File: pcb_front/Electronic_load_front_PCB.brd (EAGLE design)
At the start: 33 x 46.7 mm, 9 parts, among them SW1 EC12E_SW

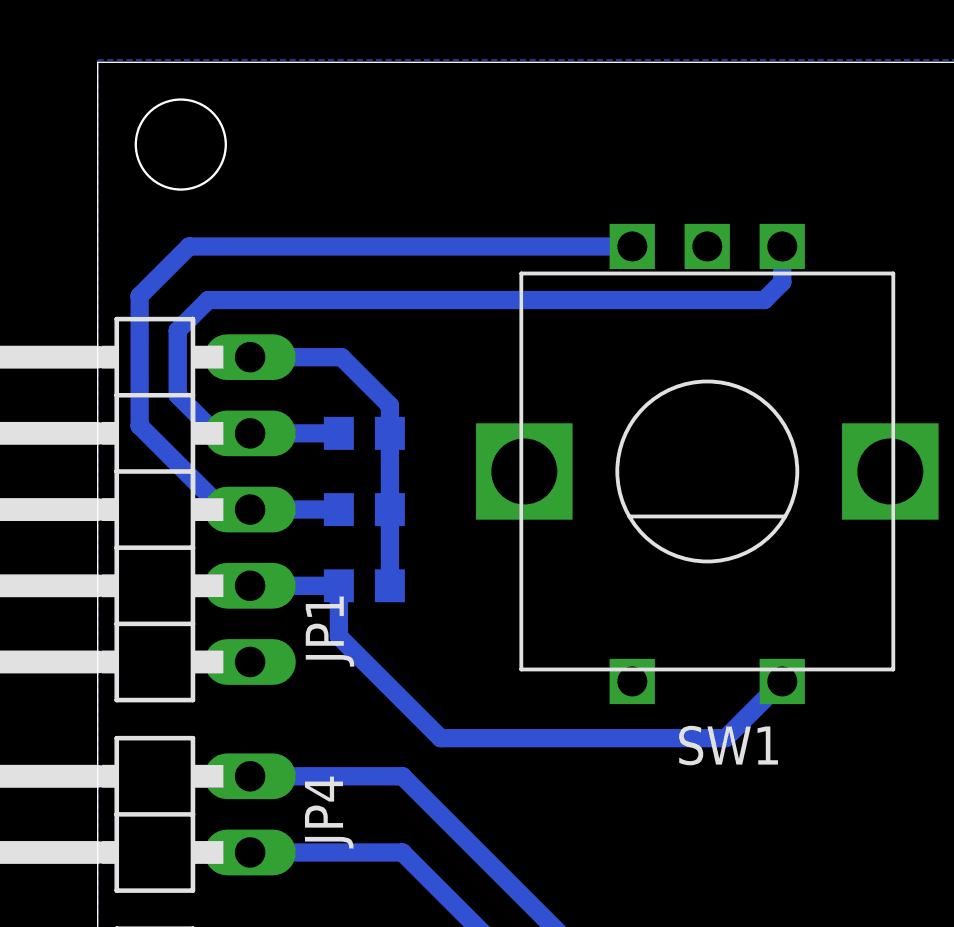
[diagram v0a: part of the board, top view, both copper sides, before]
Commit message: encoder works great, bounces reduced
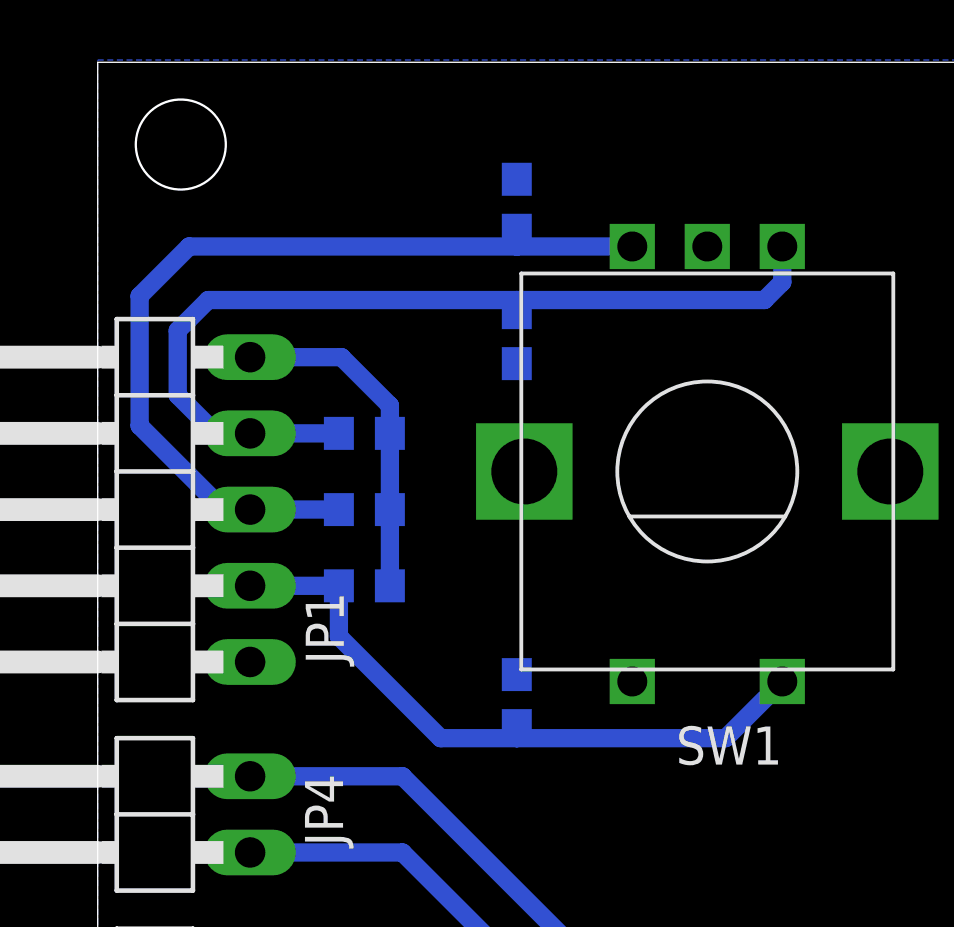
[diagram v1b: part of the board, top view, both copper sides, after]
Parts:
- added C1, C2, C3: 100n, rcl:C0603
- R1, R2: value (none) -> 4k7
- R3: value (none) -> 12k
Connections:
- net ENC_A: now also C2.1
- net ENC_B: now also C3.1
- net ENC_SW: now also C1.1
- net GND: now also C1.2, C2.2, C3.2
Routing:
- net ENC_A: track 29.2 -> 29.8 mm
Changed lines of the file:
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@@
 </layers>
 <board>
-<fusionsync huburn="a.YnVzaW5lc3M6Z21haWw1MzQ2MjM" projecturn="a.YnVzaW5lc3M6Z21haWw1MzQ2MjMjRDIwMTkxMjI5MjUwNjU0MjU2" f3durn="urn:adsk.wipprod:dm.lineage:3ZborseaTM63qMjKJInqhQ" pcbguid="" lastpulledtime="" lastsyncedchangeguid="" latestrevisionid="de9a6022-fa4f-43a6-98fc-7768da42b81b" lastsyncedrevisionid="de9a6022-fa4f-43a6-98fc-7768da42b81b" lastboardhashguid="187d4fe6-ef17-b919-9e19-ddac4a4cb30f" lastpushedtime="2022-08-03T22:12:43Z" linktopcb3d="true"/>
+<fusionsync huburn="a.YnVzaW5lc3M6Z21haWw1MzQ2MjM" projecturn="a.YnVzaW5lc3M6Z21haWw1MzQ2MjMjRDIwMTkxMjI5MjUwNjU0MjU2" f3durn="urn:adsk.wipprod:dm.lineage:3ZborseaTM63qMjKJInqhQ" pcbguid="" lastpulledtime="" lastsyncedchangeguid="" latestrevisionid="de9a6022-fa4f-43a6-98fc-7768da42b81b" lastsyncedrevisionid="de9a6022-fa4f-43a6-98fc-7768da42b81b" lastboardhashguid="187d4fe6-ef17-b919-9e19-ddac4a4cb30f" lastpushedtime="2022-08-03T22:12:43Z" linktopcb3d="false"/>
 <plain>
 <wire x1="0" y1="0" x2="33" y2="0" width="0" layer="20"/>
@@
 <attribute name="VALUE" x="4.445" y="25.4" size="1.27" layer="27" rot="R90"/>
 </element>
-<element name="R1" library="rcl" library_urn="urn:adsk.eagle:library:334" package="R0603" package3d_urn="urn:adsk.eagle:package:23555/3" value="" x="8.89" y="34.29" smashed="yes" rot="MR180">
+<element name="R1" library="rcl" library_urn="urn:adsk.eagle:library:334" package="R0603" package3d_urn="urn:adsk.eagle:package:23555/3" value="4k7" x="8.89" y="34.29" smashed="yes" rot="MR180">
 <attribute name="NAME" x="10.414" y="34.925" size="1.27" layer="26" rot="MR180"/>
 <attribute name="POPULARITY" value="70" x="8.89" y="34.29" size="1.778" layer="28" rot="MR180" display="off"/>
@@
 <attribute name="VALUE" x="8.255" y="36.195" size="1.27" layer="28" rot="MR180"/>
 </element>
-<element name="R2" library="rcl" library_urn="urn:adsk.eagle:library:334" package="R0603" package3d_urn="urn:adsk.eagle:package:23555/3" value="" x="8.89" y="31.75" smashed="yes" rot="MR180">
+<element name="R2" library="rcl" library_urn="urn:adsk.eagle:library:334" package="R0603" package3d_urn="urn:adsk.eagle:package:23555/3" value="4k7" x="8.89" y="31.75" smashed="yes" rot="MR180">
 <attribute name="NAME" x="10.414" y="32.385" size="1.27" layer="26" rot="MR180"/>
 <attribute name="POPULARITY" value="70" x="8.89" y="31.75" size="1.778" layer="28" rot="MR180" display="off"/>
@@
 <attribute name="VALUE" x="8.255" y="33.655" size="1.27" layer="28" rot="MR180"/>
 </element>
-<element name="R3" library="rcl" library_urn="urn:adsk.eagle:library:334" package="R0603" package3d_urn="urn:adsk.eagle:package:23555/3" value="" x="8.89" y="29.21" smashed="yes" rot="MR180">
+<element name="R3" library="rcl" library_urn="urn:adsk.eagle:library:334" package="R0603" package3d_urn="urn:adsk.eagle:package:23555/3" value="12k" x="8.89" y="29.21" smashed="yes" rot="MR180">
 <attribute name="NAME" x="10.414" y="29.845" size="1.27" layer="26" rot="MR180"/>
 <attribute name="POPULARITY" value="70" x="8.89" y="29.21" size="1.778" layer="28" rot="MR180" display="off"/>
@@
 <attribute name="POPULARITY" value="24" x="1.27" y="21.59" size="1.778" layer="27" rot="R90" display="off"/>
 <attribute name="VALUE" x="4.445" y="19.05" size="1.27" layer="27" rot="R90"/>
+</element>
+<element name="C1" library="rcl" library_urn="urn:adsk.eagle:library:334" package="C0603" package3d_urn="urn:adsk.eagle:package:23616/2" value="100n" x="13.97" y="25.4" smashed="yes" rot="MR90">
+<attribute name="NAME" x="11.811" y="24.257" size="1.27" layer="26" rot="MR90"/>
+<attribute name="POPULARITY" value="73" x="13.97" y="25.4" size="1.778" layer="28" rot="MR90" display="off"/>
+<attribute name="SPICEPREFIX" value="C" x="13.97" y="25.4" size="1.778" layer="28" rot="MR90" display="off"/>
+<attribute name="VALUE" x="12.065" y="24.765" size="1.27" layer="28" rot="MR90"/>
+</element>
+<element name="C2" library="rcl" library_urn="urn:adsk.eagle:library:334" package="C0603" package3d_urn="urn:adsk.eagle:package:23616/2" value="100n" x="13.97" y="41.91" smashed="yes" rot="MR90">
+<attribute name="NAME" x="11.811" y="40.767" size="1.27" layer="26" rot="MR90"/>
+<attribute name="POPULARITY" value="73" x="13.97" y="41.91" size="1.778" layer="28" rot="MR90" display="off"/>
+<attribute name="SPICEPREFIX" value="C" x="13.97" y="41.91" size="1.778" layer="28" rot="MR90" display="off"/>
+<attribute name="VALUE" x="12.065" y="41.275" size="1.27" layer="28" rot="MR90"/>
+</element>
+<element name="C3" library="rcl" library_urn="urn:adsk.eagle:library:334" package="C0603" package3d_urn="urn:adsk.eagle:package:23616/2" value="100n" x="13.97" y="37.465" smashed="yes" rot="MR270">
+<attribute name="NAME" x="11.811" y="36.195" size="1.27" layer="26" rot="MR90"/>
+<attribute name="POPULARITY" value="73" x="13.97" y="37.465" size="1.778" layer="28" rot="MR270" display="off"/>
+<attribute name="SPICEPREFIX" value="C" x="13.97" y="37.465" size="1.778" layer="28" rot="MR270" display="off"/>
+<attribute name="VALUE" x="15.875" y="38.1" size="1.27" layer="28" rot="MR270"/>
 </element>
 </elements>
@@
 <vertex x="0" y="0"/>
 </polygon>
+<contactref element="C3" pad="2"/>
+<contactref element="C2" pad="2"/>
+<contactref element="C1" pad="2"/>
 </signal>
 <signal name="5V">
@@
 <wire x1="8.04" y1="27.52" x2="11.43" y2="24.13" width="0.6096" layer="16"/>
 <wire x1="22.82" y1="26.02" x2="20.93" y2="24.13" width="0.6096" layer="16"/>
-<wire x1="20.93" y1="24.13" x2="11.43" y2="24.13" width="0.6096" layer="16"/>
+<wire x1="20.93" y1="24.13" x2="13.97" y2="24.13" width="0.6096" layer="16"/>
+<contactref element="C1" pad="1"/>
+<wire x1="13.97" y1="24.13" x2="11.43" y2="24.13" width="0.6096" layer="16"/>
+<wire x1="13.97" y1="24.55" x2="13.97" y2="24.13" width="0.6096" layer="16"/>
 </signal>
 <signal name="ENC_A">
@@
 <wire x1="4.191" y1="31.75" x2="1.397" y2="34.544" width="0.6096" layer="16"/>
 <wire x1="1.397" y1="38.869" x2="3.048" y2="40.52" width="0.6096" layer="16"/>
-<wire x1="3.048" y1="40.52" x2="17.82" y2="40.52" width="0.6096" layer="16"/>
+<wire x1="3.048" y1="40.52" x2="13.97" y2="40.52" width="0.6096" layer="16"/>
+<wire x1="13.97" y1="40.52" x2="17.82" y2="40.52" width="0.6096" layer="16"/>
 <wire x1="1.397" y1="34.544" x2="1.397" y2="38.869" width="0.6096" layer="16"/>
+<contactref element="C2" pad="1"/>
+<wire x1="13.97" y1="41.06" x2="13.97" y2="40.52" width="0.6096" layer="16"/>
 </signal>
 <signal name="ENC_B">
@@
 <wire x1="22.225" y1="38.735" x2="22.82" y2="39.33" width="0.6096" layer="16"/>
 <wire x1="22.82" y1="39.33" x2="22.82" y2="40.52" width="0.6096" layer="16"/>
-<wire x1="3.683" y1="38.735" x2="22.225" y2="38.735" width="0.6096" layer="16"/>
+<wire x1="3.683" y1="38.735" x2="13.97" y2="38.735" width="0.6096" layer="16"/>
+<contactref element="C3" pad="1"/>
+<wire x1="13.97" y1="38.735" x2="22.225" y2="38.735" width="0.6096" layer="16"/>
+<wire x1="13.97" y1="38.315" x2="13.97" y2="38.735" width="0.6096" layer="16"/>
 </signal>
 <signal name="N$1">
